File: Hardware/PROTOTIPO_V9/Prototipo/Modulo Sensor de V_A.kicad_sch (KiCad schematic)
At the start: 0 parts

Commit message: Esquematico TR V 1 ,2 & 3
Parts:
- added J1, J2, J3: Screw_Terminal_01x02, symbol Connector:Screw_Terminal_01x02
- added U2, U3, U4: zmpt101b, symbol zmpt101b:zmpt101b
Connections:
- new net +5V: U2.5 (VCC), U3.5 (VCC), U4.5 (VCC)
- new net GND: U2.3 (GND), U2.4 (GND), U3.3 (GND), U3.4 (GND), U4.3 (GND), U4.4 (GND)
- new net OUT_TR_V_1: U2.6 (OUT)
- new net OUT_TR_V_2: U3.6 (OUT)
- new net OUT_TR_V_3: U4.6 (OUT)
- new net TR_V_1_L: J1.2 (Pin_2), U2.1 (L)
- new net TR_V_1_N: J1.1 (Pin_1), U2.2 (N)
- new net TR_V_2_L: J2.2 (Pin_2), U3.1 (L)
- new net TR_V_2_N: J2.1 (Pin_1), U3.2 (N)
- new net TR_V_3_L: J3.2 (Pin_2), U4.1 (L)
- new net TR_V_3_N: J3.1 (Pin_1), U4.2 (N)

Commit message: Esquematico RTC
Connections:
- net TR_V_1_L renamed 220VAC_L
- net TR_V_1_N renamed 220VAC_N
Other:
- moved on the sheet: J1, J2, J3
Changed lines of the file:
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@@
 	(paper "A4")
+	(junction
+		(at 99.06 54.61)
+		(diameter 0)
+		(color 0 0 0 0)
+	)
 	(junction
 		(at 146.05 64.77)
@@
 	)
 	(junction
+		(at 101.6 52.07)
+		(diameter 0)
+		(color 0 0 0 0)
+	)
+	(junction
 		(at 146.05 95.25)
 		(diameter 0)
@@
 	(wire
 		(pts
-			(xy 115.57 114.3) (xy 135.89 114.3)
+			(xy 80.01 114.3) (xy 135.89 114.3)
 		)
 		(stroke
@@
 	(wire
 		(pts
+			(xy 92.71 41.91) (xy 99.06 41.91)
+		)
+		(stroke
+			(width 0)
+			(type default)
+		)
+	)
+	(wire
+		(pts
+			(xy 92.71 38.1) (xy 101.6 38.1)
+		)
+		(stroke
+			(width 0)
+			(type default)
+		)
+	)
+	(wire
+		(pts
 			(xy 172.72 95.25) (xy 172.72 87.63)
 		)
@@
 	(wire
 		(pts
-			(xy 115.57 82.55) (xy 135.89 82.55)
+			(xy 80.01 82.55) (xy 135.89 82.55)
+		)
+		(stroke
+			(width 0)
+			(type default)
+		)
+	)
+	(wire
+		(pts
+			(xy 101.6 38.1) (xy 101.6 52.07)
 		)
 		(stroke
@@
 	(wire
 		(pts
+			(xy 101.6 52.07) (xy 135.89 52.07)
+		)
+		(stroke
+			(width 0)
+			(type default)
+		)
+	)
+	(wire
+		(pts
 			(xy 172.72 111.76) (xy 195.58 111.76)
 		)
@@
 	(wire
 		(pts
-			(xy 115.57 116.84) (xy 135.89 116.84)
+			(xy 80.01 116.84) (xy 135.89 116.84)
 		)
 		(stroke
@@
 	(wire
 		(pts
+			(xy 99.06 54.61) (xy 135.89 54.61)
+		)
+		(stroke
+			(width 0)
+			(type default)
+		)
+	)
+	(wire
+		(pts
 			(xy 144.78 101.6) (xy 172.72 101.6)
 		)
@@
 	(wire
 		(pts
-			(xy 115.57 85.09) (xy 135.89 85.09)
+			(xy 80.01 85.09) (xy 135.89 85.09)
+		)
+		(stroke
+			(width 0)
+			(type default)
+		)
+	)
+	(wire
+		(pts
+			(xy 99.06 41.91) (xy 99.06 54.61)
 		)
 		(stroke
@@
 	(wire
 		(pts
-			(xy 115.57 54.61) (xy 135.89 54.61)
-		)
-		(stroke
-			(width 0)
-			(type default)
-		)
-	)
-	(wire
-		(pts
-			(xy 115.57 52.07) (xy 135.89 52.07)
+			(xy 80.01 54.61) (xy 99.06 54.61)
+		)
+		(stroke
+			(width 0)
+			(type default)
+		)
+	)
+	(wire
+		(pts
+			(xy 80.01 52.07) (xy 101.6 52.07)
 		)
 		(stroke
@@
 		)
 	)
+	(hierarchical_label "220VAC_N"
+		(shape output)
+		(at 92.71 41.91 180)
+		(effects
+			(font
+				(size 1.27 1.27)
+			)
+			(justify right)
+		)
+	)
 	(hierarchical_label "OUT_TR_V_2"
 		(shape output)
@@
 		)
 	)
+	(hierarchical_label "220VAC_L"
+		(shape output)
+		(at 92.71 38.1 180)
+		(effects
+			(font
+				(size 1.27 1.27)
+			)
+			(justify right)
+		)
+	)
 	(hierarchical_label "OUT_TR_V_3"
 		(shape output)
@@
 	(symbol
 		(lib_id "Connector:Screw_Terminal_01x02")
-		(at 110.49 54.61 180)
+		(at 74.93 54.61 180)
 		(unit 1)
 		(exclude_from_sim no)
@@
 		(fields_autoplaced yes)
 		(property "Reference" "J1"
-			(at 110.49 45.72 0)
+			(at 74.93 45.72 0)
 			(effects
 				(font
@@
 		)
 		(property "Value" "Screw_Terminal_01x02"
-			(at 110.49 48.26 0)
+			(at 74.93 48.26 0)
 			(effects
 				(font
@@
 		)
 		(property "Footprint" ""
-			(at 110.49 54.61 0)
+			(at 74.93 54.61 0)
 			(effects
 				(font
@@
 		)
 		(property "Datasheet" "~"
-			(at 110.49 54.61 0)
+			(at 74.93 54.61 0)
 			(effects
 				(font
@@
 		)
 		(property "Description" "Generic screw terminal, single row, 01x02, script generated (kicad-library-utils/schlib/autogen/connector/)"
-			(at 110.49 54.61 0)
+			(at 74.93 54.61 0)
 			(effects
 				(font
@@
 	(symbol
 		(lib_id "Connector:Screw_Terminal_01x02")
-		(at 110.49 85.09 180)
+		(at 74.93 85.09 180)
 		(unit 1)
 		(exclude_from_sim no)
@@
 		(fields_autoplaced yes)
 		(property "Reference" "J2"
-			(at 110.49 76.2 0)
+			(at 74.93 76.2 0)
 			(effects
 				(font
@@
 		)
 		(property "Value" "Screw_Terminal_01x02"
-			(at 110.49 78.74 0)
+			(at 74.93 78.74 0)
 			(effects
 				(font
@@
 		)
 		(property "Footprint" ""
-			(at 110.49 85.09 0)
+			(at 74.93 85.09 0)
 			(effects
 				(font
@@
 		)
 		(property "Datasheet" "~"
-			(at 110.49 85.09 0)
+			(at 74.93 85.09 0)
 			(effects
 				(font
@@
 		)
 		(property "Description" "Generic screw terminal, single row, 01x02, script generated (kicad-library-utils/schlib/autogen/connector/)"
-			(at 110.49 85.09 0)
+			(at 74.93 85.09 0)
 			(effects
 				(font
@@
 	(symbol
 		(lib_id "Connector:Screw_Terminal_01x02")
-		(at 110.49 116.84 180)
+		(at 74.93 116.84 180)
 		(unit 1)
 		(exclude_from_sim no)
@@
 		(fields_autoplaced yes)
 		(property "Reference" "J3"
-			(at 110.49 107.95 0)
+			(at 74.93 107.95 0)
 			(effects
 				(font
@@
 		)
 		(property "Value" "Screw_Terminal_01x02"
-			(at 110.49 110.49 0)
+			(at 74.93 110.49 0)
 			(effects
 				(font
@@
 		)
 		(property "Footprint" ""
-			(at 110.49 116.84 0)
+			(at 74.93 116.84 0)
 			(effects
 				(font
@@
 		)
 		(property "Datasheet" "~"
-			(at 110.49 116.84 0)
+			(at 74.93 116.84 0)
 			(effects
 				(font
@@
 		)
 		(property "Description" "Generic screw terminal, single row, 01x02, script generated (kicad-library-utils/schlib/autogen/connector/)"
-			(at 110.49 116.84 0)
-			(effects
-				(font
+			(at 74.93 116.84 0)
+			(effects
+				(font

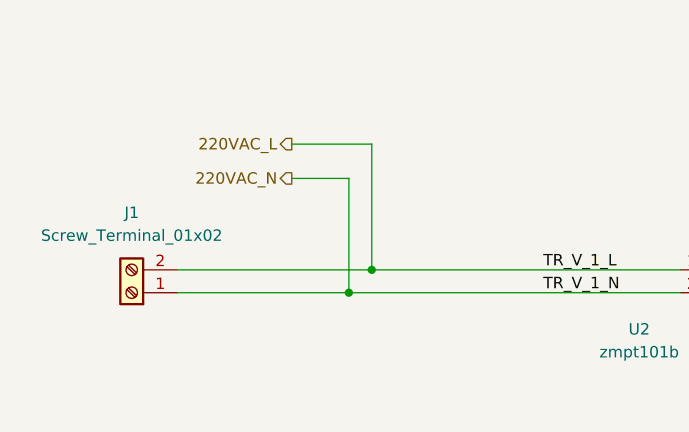
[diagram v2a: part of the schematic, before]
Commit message: ERC: 0 errores
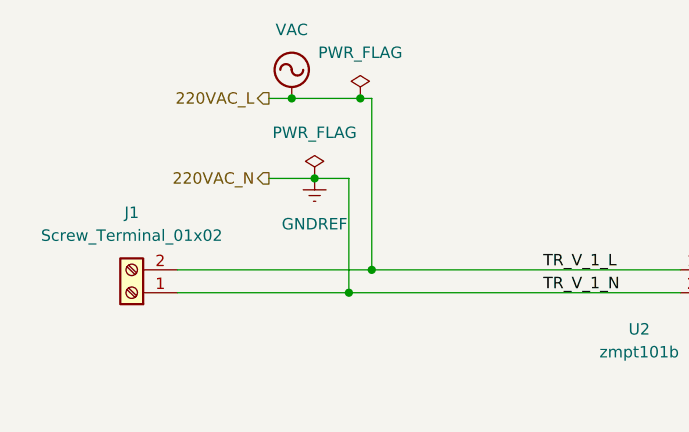
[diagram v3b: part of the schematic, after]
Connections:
- net 220VAC_L renamed VAC
- net 220VAC_N renamed GNDREF

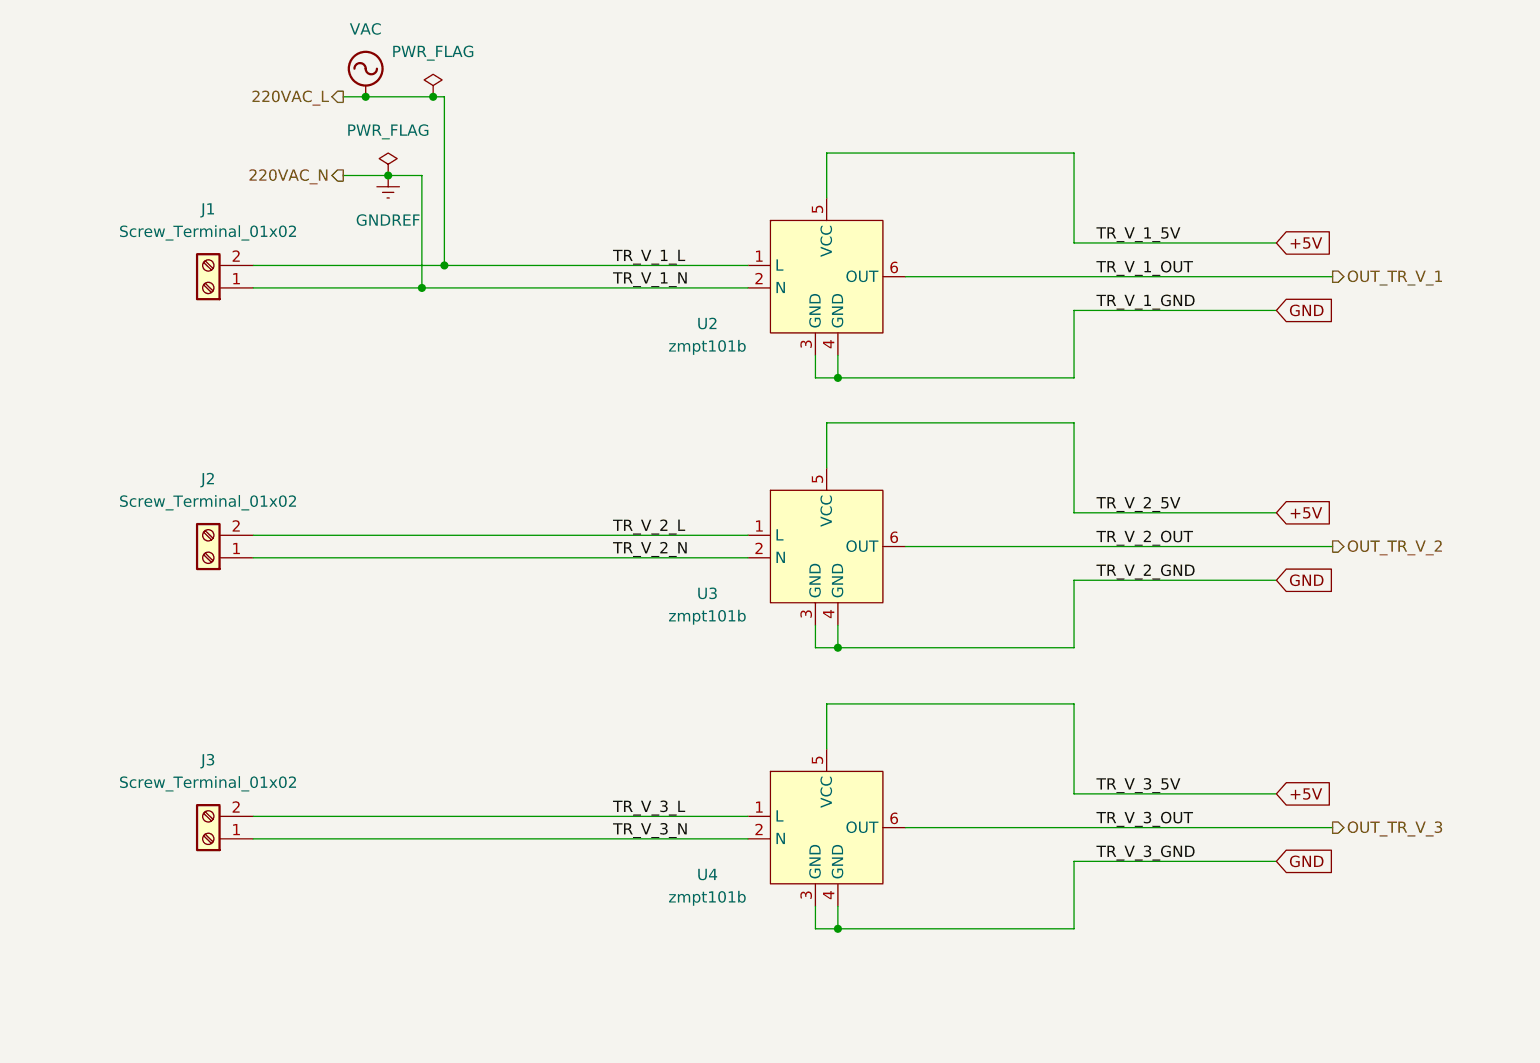
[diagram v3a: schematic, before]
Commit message: Asignación de huellas
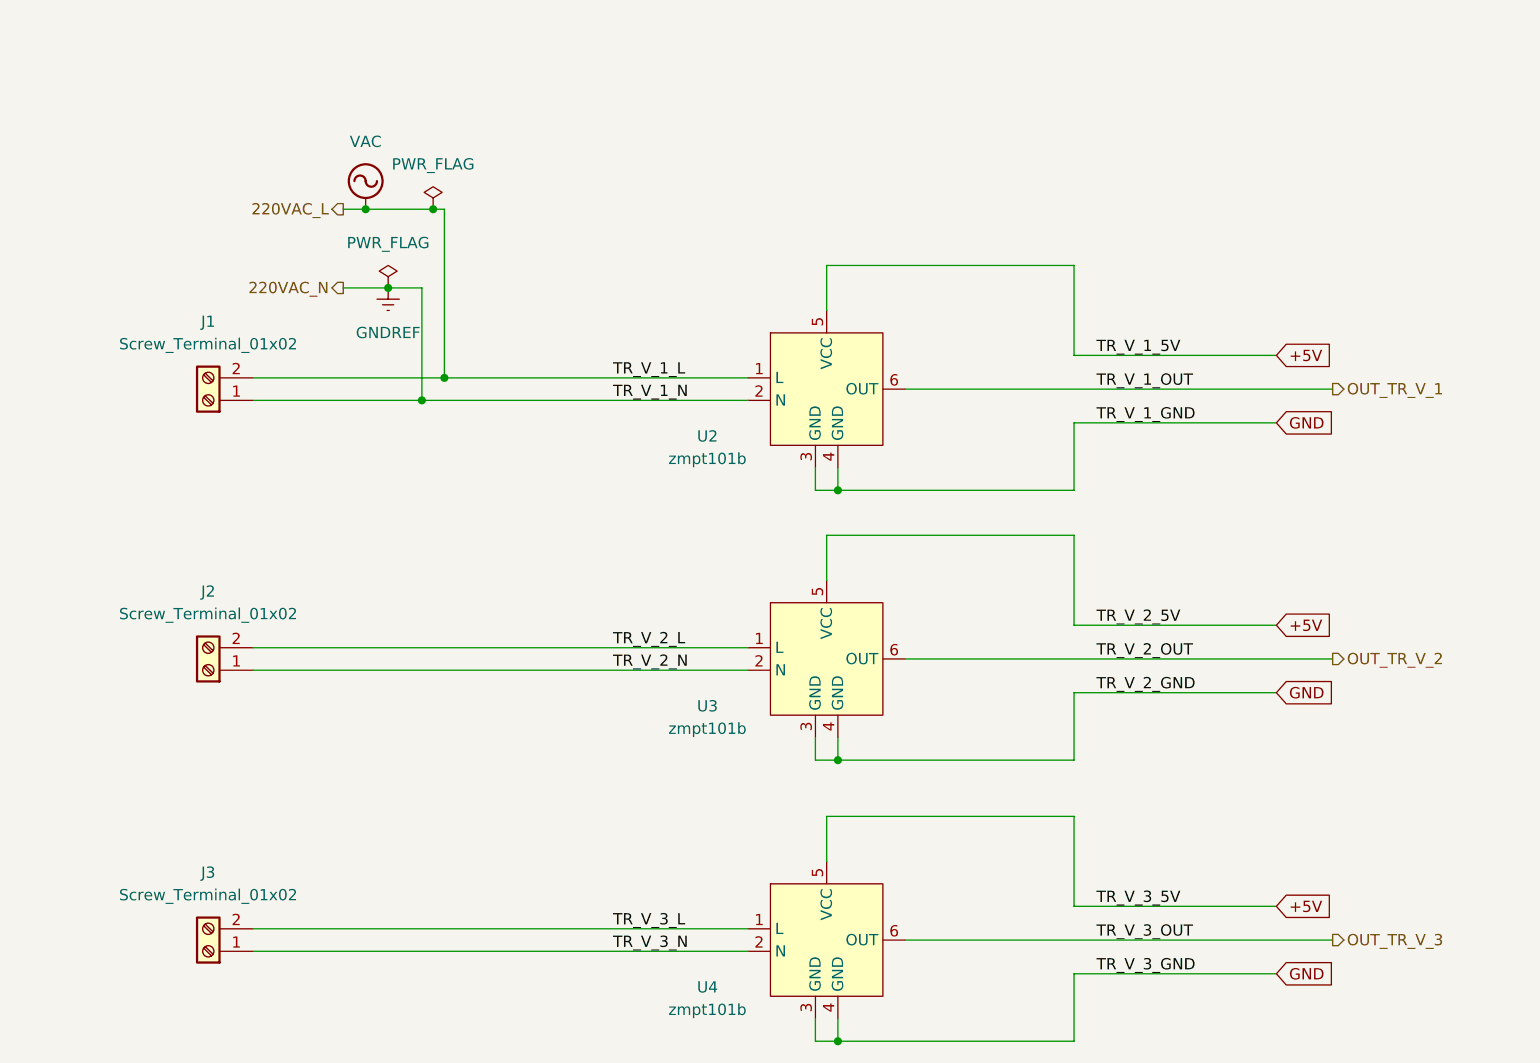
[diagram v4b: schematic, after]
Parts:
- J1, J2, J3: footprint (none) -> TerminalBlock:TerminalBlock_Xinya_XY308-2.54-2P_1x02_P2.54mm_Horizontal
- U2, U3, U4: footprint (none) -> Connector_PinSocket_2.54mm:PinSocket_1x04_P2.54mm_Vertical
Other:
- moved on the sheet: J1, J2, J3, U2, U3, U4

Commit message: Esquematico TR de Corriente
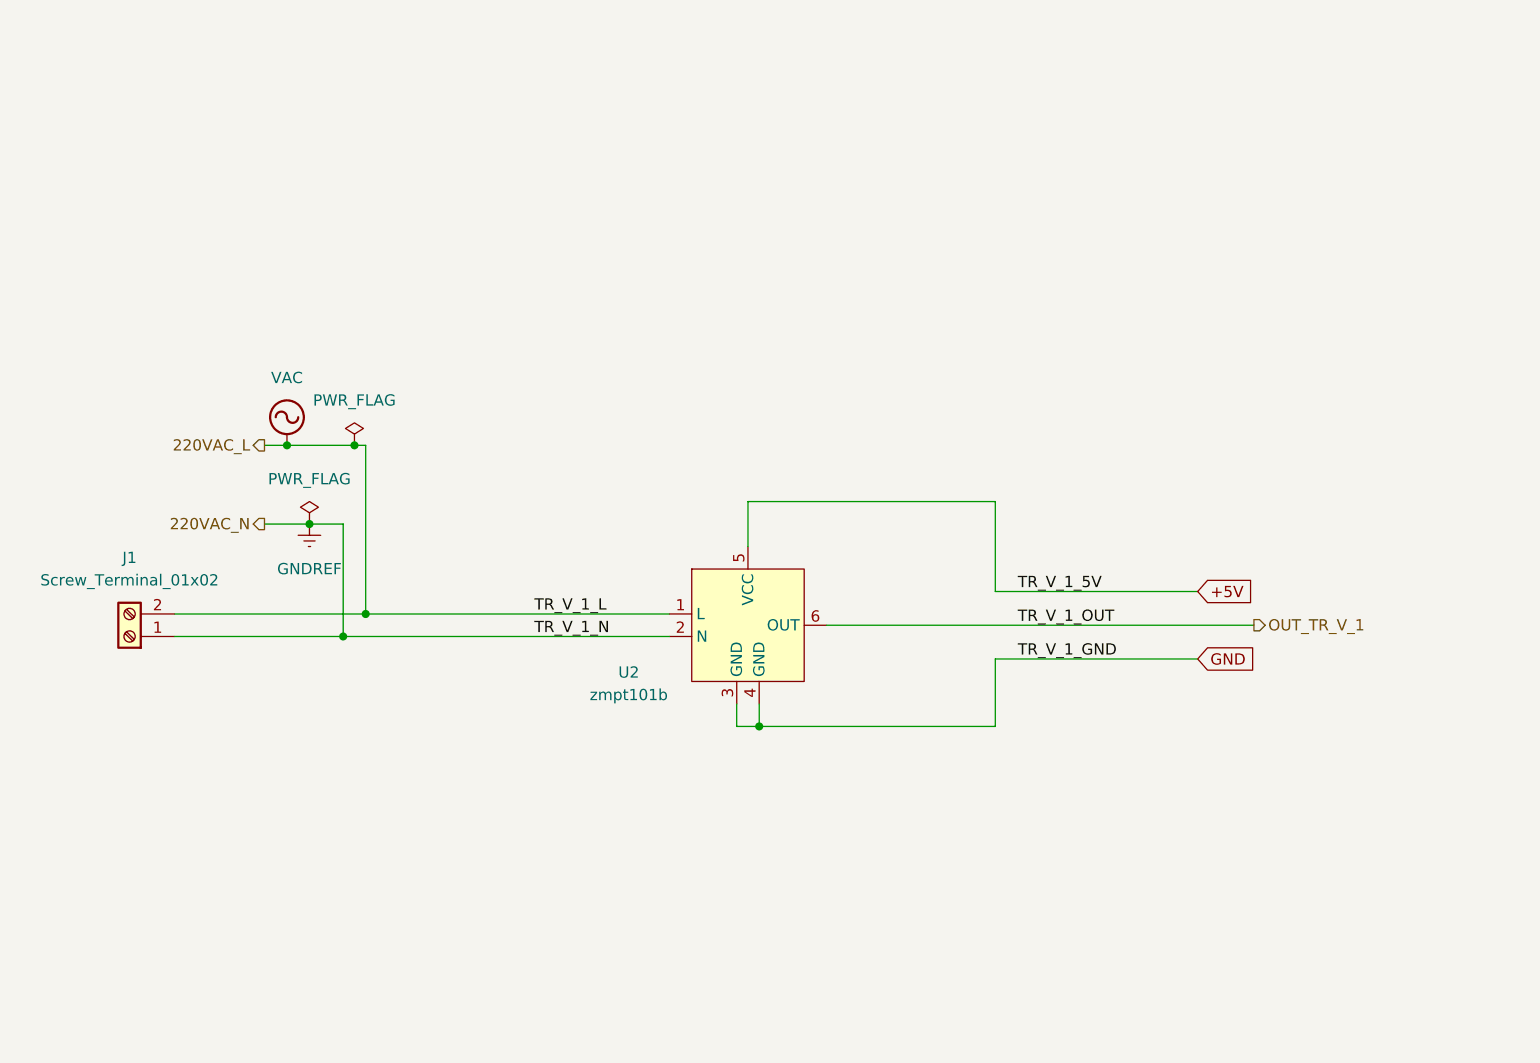
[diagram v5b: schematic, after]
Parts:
- removed J2, J3: Screw_Terminal_01x02, TerminalBlock:TerminalBlock_Xinya_XY308-2.54-2P_1x02_P2.54mm_Horizontal, symbol Connector:Screw_Terminal_01x02
- removed U3, U4: zmpt101b, Connector_PinSocket_2.54mm:PinSocket_1x04_P2.54mm_Vertical, symbol zmpt101b:zmpt101b
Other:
- moved on the sheet: J1, U2

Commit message: Esquematico completo v1.0
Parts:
- added C4: 10u, symbol Device:C_Polarized
- added R17: 10k, symbol Device:R
- added R18: 10K, symbol Device:R
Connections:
- net +5V: now also R17.2
- net GND: now also C4.2, R18.2
- net GNDREF renamed 220VAC_N
- net OUT_TR_V_1 renamed OUT_TR_V_1+
- net VAC renamed 220VAC_L
- new net OUT_TR_V_1-: C4.1, R17.1, R18.1

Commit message: Footprints asignados
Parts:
- C4: footprint (none) -> Capacitor_THT:CP_Radial_D5.0mm_P2.50mm
- R17, R18: footprint (none) -> Resistor_THT:R_Axial_DIN0207_L6.3mm_D2.5mm_P10.16mm_Horizontal
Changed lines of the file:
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@@
 			)
 		)
-		(property "Footprint" ""
+		(property "Footprint" "Resistor_THT:R_Axial_DIN0207_L6.3mm_D2.5mm_P10.16mm_Horizontal"
 			(at 176.022 72.39 90)
 			(effects
@@
 			)
 		)
-		(property "Footprint" ""
+		(property "Footprint" "Resistor_THT:R_Axial_DIN0207_L6.3mm_D2.5mm_P10.16mm_Horizontal"
 			(at 179.578 62.23 90)
 			(effects
@@
 			)
 		)
-		(property "Footprint" ""
+		(property "Footprint" "Capacitor_THT:CP_Radial_D5.0mm_P2.50mm"
 			(at 188.9252 76.2 0)
 			(effects

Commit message: fp definitivos - Planteo de PCB con componentes
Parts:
- U2: footprint Connector_PinSocket_2.54mm:PinSocket_1x04_P2.54mm_Vertical -> footprints_proyecto:MODULE_ZMPT101B
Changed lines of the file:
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@@
 			)
 		)
-		(property "Footprint" "Connector_PinSocket_2.54mm:PinSocket_1x04_P2.54mm_Vertical"
+		(property "Footprint" "footprints_proyecto:MODULE_ZMPT101B"
 			(at 138.43 92.71 0)
 			(effects
